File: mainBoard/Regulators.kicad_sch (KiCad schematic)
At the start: 20 parts, among them IC2 LT8631IFE#PBF, J18 1935161

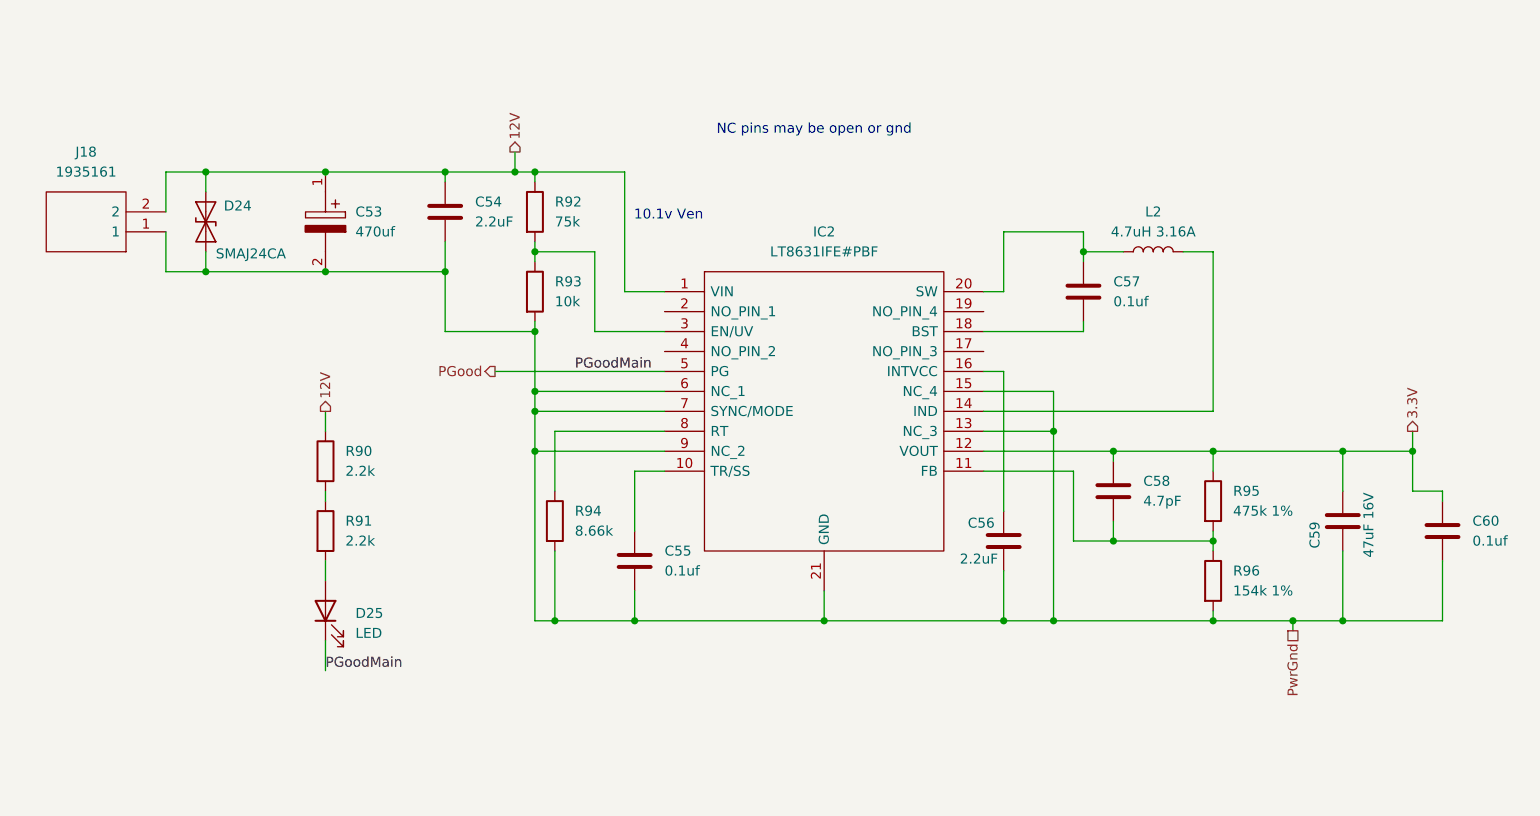
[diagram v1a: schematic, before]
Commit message: need to finish new regulators and run parts check on sch
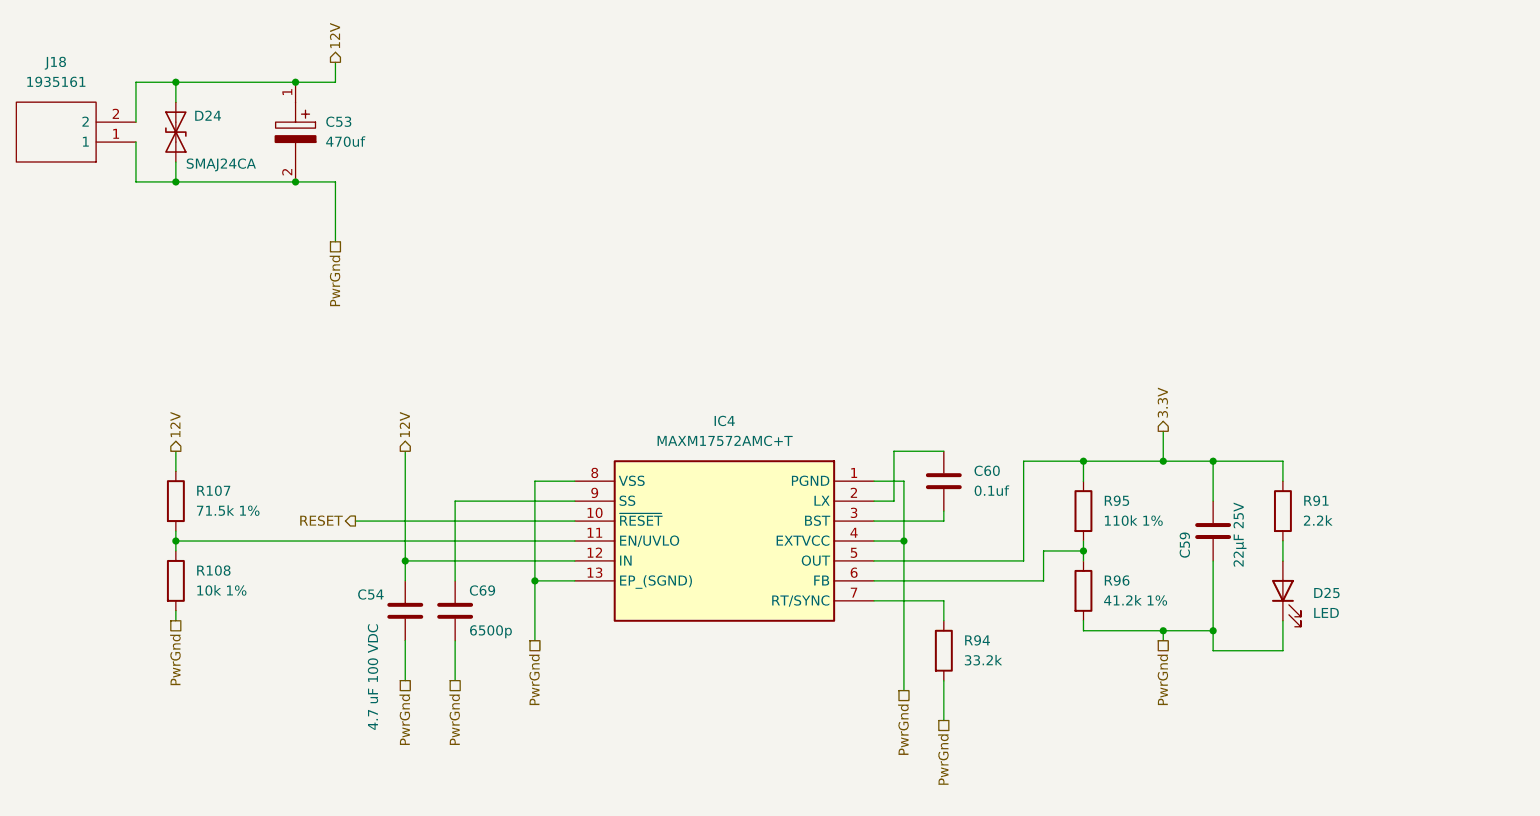
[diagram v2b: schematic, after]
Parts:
- removed C55, C57: 0.1uf, Capacitor_SMD:C_0402_1005Metric, symbol Device:C
- removed C56: 2.2uF, Capacitor_SMD:C_1206_3216Metric, symbol Device:C
- removed C58: 4.7pF, Capacitor_SMD:C_0402_1005Metric, symbol Device:C
- removed IC2: LT8631IFE#PBF, SamacSys_Parts:SOP65P640X120-21N, symbol SamacSys_Parts:LT8631IFE#PBF
- removed L2: 4.7uH 3.16A, Inductor_SMD:L_7.3x7.3_H4.5, symbol Device:L
- removed R90: 2.2k, Resistor_SMD:R_0805_2012Metric, symbol Device:R
- removed R92: 75k, Resistor_SMD:R_0402_1005Metric, symbol Device:R
- removed R93: 10k, Resistor_SMD:R_0402_1005Metric, symbol Device:R
- added C69: 6500p, Capacitor_SMD:C_0402_1005Metric, symbol Device:C
- added IC4: MAXM17572AMC+T, parts:MAXM17572AMC, symbol MAXM17572AMC+T:MAXM17572AMC+T
- added R107: 71.5k 1%, Resistor_SMD:R_0402_1005Metric, symbol Device:R
- added R108: 10k 1%, Resistor_SMD:R_0402_1005Metric, symbol Device:R
- C54: value 2.2uF -> 4.7 uF 100 VDC; Mouser https://www.mouser.com/ProductDetail/Samsung-Electro-Mechan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 -> https://www.mouser.com/en/ProductDetail/Murata-Electronics/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; Mouser Part Number Alt https://www.mouser.com/en/ProductDetail/Samsung-Electro-Mec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 -> https://www.mouser.com/en/ProductDetail/Murata-Electronics/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; Mouser Part Number Alt 2 https://www.mouser.com/en/ProductDetail/Murata-Electronics/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 -> (none); Mouser Part Number Alt 3 https://www.mouser.com/en/ProductDetail/Murata-Electronics/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 -> (none); Mouser Part Number Alt 4 https://www.mouser.com/en/ProductDetail/KEMET/C1206C225K5RA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 -> (none)
- C59: value 47uF 16V -> 22μF 25V; Mouser https://www.mouser.com/en/ProductDetail/Samsung-Electro-Mechanics/CL32A476KOJNNNE?qs=d72FGnIDsgQXYP%252BbBe7Sww%3D%3D -> https://www.mouser.com/en/ProductDetail/Samsung-Electro-Mechanics/CL32B226KAJNNNE?qs=349EhDEZ59oxUqah7LWaWw%3D%3D
- R94: value 8.66k -> 33.2k
- R95: value 475k 1% -> 110k 1%
- R96: value 154k 1% -> 41.2k 1%
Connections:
- net PGood is gone; now on net PwrGnd: D25.1 (K)
- net 12V: now also IC4.12 (IN), R107.1
- net 3.3V: now also R91.1, IC4.5 (OUT); no longer C60.1
- net PwrGnd: now also C69.2, IC4.1 (PGND), IC4.13 (EP_(SGND)), IC4.4 (EXTVCC), IC4.8 (VSS), R108.2; no longer C60.2
- net at R95.2, R96.1: now also IC4.6 (FB)
- net at R94.1: now also IC4.7 (RT/SYNC)
- new net: IC4.11 (EN/UVLO), R107.2, R108.1
- new net: C60.1, IC4.2 (LX)
- new net: C60.2, IC4.3 (BST)
- new net: C69.1, IC4.9 (SS)
- new net RESET: IC4.10 (~{RESET})
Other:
- note removed: "10.1v Ven"
- note removed: "NC pins may be open or gnd"
- moved on the sheet: C53, C54, D24, J18, R94

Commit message: almost done
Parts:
- added C13: 2.2uF, Capacitor_SMD:C_1206_3216Metric, symbol Device:C
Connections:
- net PwrGnd: now also C13.2; no longer IC4.8 (VSS)
- new net: C13.1, IC4.8 (VCC)
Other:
- moved on the sheet: C54, C69, R107, R108

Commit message: i think the pcbs and sch are good
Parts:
- C69: value 6500p -> 6800p; Manufacturer_Name (none) -> Murata Electronics; Manufacturer_Part_Number (none) -> GRM1555C1H682GE01D; Mouser Part Number (none) -> https://www.mouser.com/en/ProductDetail/Murata-Electronics/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
- R107: Manufacturer_Part_Number (none) -> CRCW040271K5FKED
- R108: Manufacturer_Part_Number (none) -> CRCW040210K0FKED
- R94: Manufacturer_Part_Number (none) -> CRCW040233K2FKED
- R95: Manufacturer_Part_Number (none) -> CRCW0402110KFKED
- R96: Manufacturer_Part_Number (none) -> CRCW040241K2FKED
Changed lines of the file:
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@@
 			)
 		)
-		(property "Datasheet" "https://www.mouser.com/ProductDetail/Vishay/CRCW0402422KFKED?qs=rzhQWu8UUS38CTZyFvhEkw%3D%3D"
+		(property "Datasheet" "https://www.mouser.com/en/ProductDetail/Vishay/CRCW0402110KFKED?qs=rlE3Te1NifyoK3%2FXIabNHA%3D%3D"
+			(at 217.17 83.82 0)
+			(hide yes)
+			(show_name no)
+			(do_not_autoplace no)
+			(effects
+				(font
+					(size 1.27 1.27)
+				)
+			)
+		)
+		(property "Manufacturer_Part_Number" "CRCW0402110KFKED"
 			(at 217.17 83.82 0)
 			(hide yes)
@@
 			)
 		)
-		(property "Datasheet" "https://www.mouser.com/ProductDetail/Vishay/CRCW0402422KFKED?qs=rzhQWu8UUS38CTZyFvhEkw%3D%3D"
+		(property "Datasheet" "https://www.mouser.com/en/ProductDetail/Vishay/CRCW040271K5FKED?qs=Yor07UEv01XW6Jak8uNg1A%3D%3D"
+			(at 99.06 82.55 0)
+			(hide yes)
+			(show_name no)
+			(do_not_autoplace no)
+			(effects
+				(font
+					(size 1.27 1.27)
+				)
+			)
+		)
+		(property "Manufacturer_Part_Number" "CRCW040271K5FKED"
 			(at 99.06 82.55 0)
 			(hide yes)
@@
 			)
 		)
-		(property "Datasheet" "https://www.mouser.com/ProductDetail/Vishay/CRCW04028K66FKEDC?qs=E3Y5ESvWgWPo4%2Fhc%252BAkQtg%3D%3D"
+		(property "Datasheet" "https://www.mouser.com/en/ProductDetail/Vishay/CRCW040233K2FKED?qs=TNtMkGKFKOxaNJ4fnQ3loQ%3D%3D"
+			(at 199.39 101.6 0)
+			(hide yes)
+			(show_name no)
+			(do_not_autoplace no)
+			(effects
+				(font
+					(size 1.27 1.27)
+				)
+			)
+		)
+		(property "Manufacturer_Part_Number" "CRCW040233K2FKED"
 			(at 199.39 101.6 0)
 			(hide yes)
@@
 			)
 		)
-		(property "Datasheet" "https://www.mouser.com/en/ProductDetail/Vishay/CRCW0402154KFKED?qs=sGAEpiMZZMtlubZbdhIBICyxlhGRQNJfRCzUCssnsug%3D"
+		(property "Datasheet" "https://www.mouser.com/en/ProductDetail/Vishay/CRCW040241K2FKED?qs=rzhQWu8UUS3cUU8DfR1cag%3D%3D"
+			(at 217.17 93.98 0)
+			(hide yes)
+			(show_name no)
+			(do_not_autoplace no)
+			(effects
+				(font
+					(size 1.27 1.27)
+				)
+			)
+		)
+		(property "Manufacturer_Part_Number" "CRCW040241K2FKED"
 			(at 217.17 93.98 0)
 			(hide yes)
@@
 			)
 		)
-		(property "Datasheet" "https://www.mouser.com/en/ProductDetail/Vishay/CRCW0402154KFKED?qs=sGAEpiMZZMtlubZbdhIBICyxlhGRQNJfRCzUCssnsug%3D"
+		(property "Datasheet" "https://www.mouser.com/en/ProductDetail/Vishay/CRCW040210K0FKED?qs=rlE3Te1NifyN3e8vvxacSw%3D%3D"
+			(at 99.06 92.71 0)
+			(hide yes)
+			(show_name no)
+			(do_not_autoplace no)
+			(effects
+				(font
+					(size 1.27 1.27)
+				)
+			)
+		)
+		(property "Manufacturer_Part_Number" "CRCW040210K0FKED"
 			(at 99.06 92.71 0)
 			(hide yes)
@@
 			)
 		)
-		(property "Value" "6500p"
+		(property "Value" "6800p"
 			(at 144.018 99.06 0)
 			(show_name no)
@@
 			)
 		)
-		(property "Datasheet" "https://www.mouser.com/en/ProductDetail/Murata-Electronics/GCM155R71H104KE02J?qs=hNud%2FORuBR1wlwGPFWBVDg%3D%3D"
+		(property "Datasheet" "https://www.mouser.com/en/ProductDetail/Murata-Electronics/GRM1555C1H682GE01D?qs=d0WKAl%252BL4KZmZL9n8aRONA%3D%3D"
 			(at 142.24 96.52 0)
 			(hide yes)
+			(show_name no)
+			(do_not_autoplace no)
+			(effects
+				(font
+					(size 1.27 1.27)
+				)
+			)
+		)
+		(property "Mouser Part Number" "https://www.mouser.com/en/ProductDetail/Murata-Electronics/GRM1555C1H682GE01D?qs=d0WKAl%252BL4KZmZL9n8aRONA%3D%3D"
+			(at 142.24 96.52 0)
+			(hide yes)
+			(show_name no)
+			(do_not_autoplace no)
+			(effects
+				(font
+					(size 1.27 1.27)
+				)
+			)
+		)
+		(property "Manufacturer_Part_Number" "GRM1555C1H682GE01D"
+			(at 142.24 96.52 0)
+			(hide yes)
+			(show_name no)
+			(do_not_autoplace no)
+			(effects
+				(font
+					(size 1.27 1.27)
+				)
+			)
+		)
+		(property "Manufacturer_Name" "Murata Electronics"
+			(at 142.24 96.52 0)
+			(hide yes)
